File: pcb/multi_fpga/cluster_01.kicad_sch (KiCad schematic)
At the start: 4 parts

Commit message: Fixed library and power issues.
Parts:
- A2: symbol CMOD_S7 -> multi_fpga:CMOD_S7
- C25, C26: symbol C -> multi_fpga:C
- VR1: symbol LDO_1V8 -> Regulator_Linear:MCP1700x-180xxTT
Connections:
- net +5V: no longer VR1.3 (IN)
- net C1_1V8: no longer VR1.2 (OUT)
- net GND: no longer VR1.1 (GND)
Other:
- moved on the sheet: VR1
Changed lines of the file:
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@@
 	)
 	(symbol
-		(lib_id "power:C1_1V8")
+		(lib_id "multi_fpga:C1_1V8")
 		(at 270.51 213.36 0)
 		(unit 1)
@@
 	)
 	(symbol
-		(lib_id "LDO_1V8")
+		(lib_id "Regulator_Linear:MCP1700x-180xxTT")
 		(at 300.99 218.44 0)
 		(unit 1)
@@
 	)
 	(symbol
-		(lib_id "C")
+		(lib_id "multi_fpga:C")
 		(at 326.39 218.44 0)
 		(unit 1)
@@
 	)
 	(symbol
-		(lib_id "power:C1_1V8")
+		(lib_id "multi_fpga:C1_1V8")
 		(at 326.39 214.63 0)
 		(unit 1)
@@
 	)
 	(symbol
-		(lib_id "CMOD_S7")
+		(lib_id "multi_fpga:CMOD_S7")
 		(at 262.89 142.24 0)
 		(unit 1)
@@
 	)
 	(symbol
-		(lib_id "C")
+		(lib_id "multi_fpga:C")
 		(at 255.27 218.44 0)
 		(unit 1)

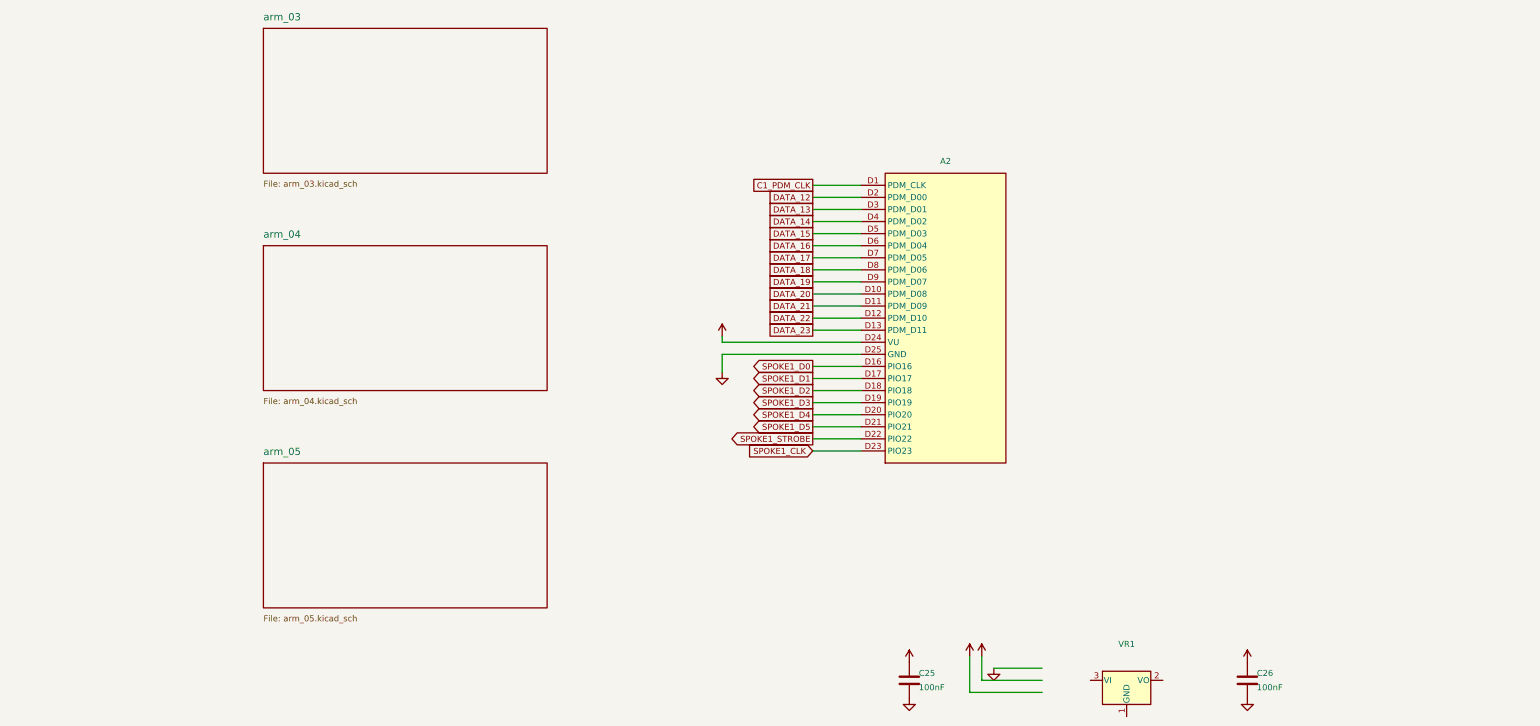
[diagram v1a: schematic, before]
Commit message: Fixed power and C ref des collisions.
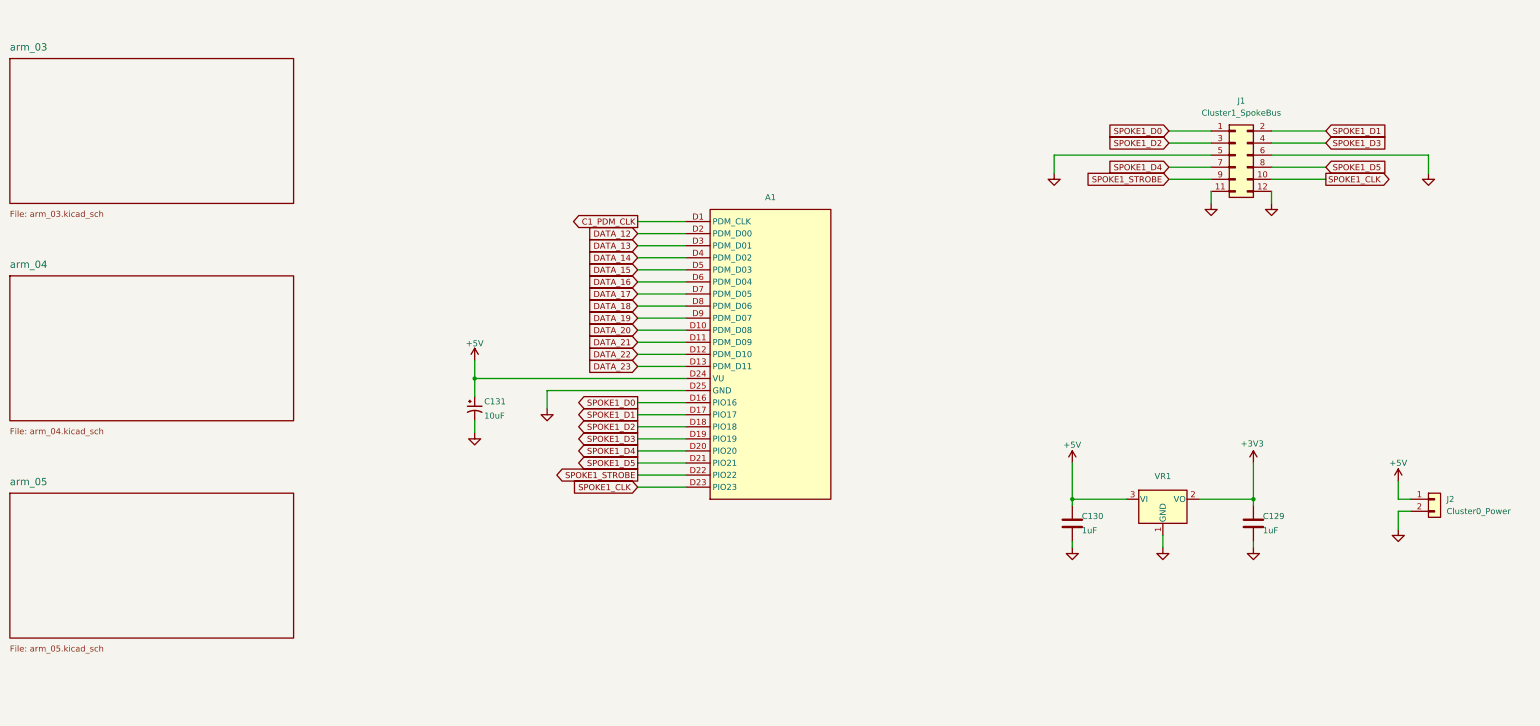
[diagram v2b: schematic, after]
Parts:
- removed C25, C26: 100nF, symbol multi_fpga:C
- added C129, C130: 1uF, Capacitor_SMD:C_0201_0603Metric, symbol multi_fpga:C
- added C131: 10uF, SparkFun-Capacitor:C_0603_1608Metric_Polar, symbol SparkFun-Capacitor:10uF_0603_6.3V_20%_Polar(Tant)
- added J1: Cluster1_SpokeBus, Connector_PinHeader_2.54mm:PinHeader_2x06_P2.54mm_Vertical, symbol Connector_Generic:Conn_02x06_Odd_Even
- added J2: Cluster0_Power, symbol Connector_Generic:Conn_01x02
- renumbered A2 to A1
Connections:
- net +5V: now also VR1.3 (VI), C130.1, C131.1, J2.1 (Pin_1)
- net GND: now also VR1.1 (GND), C129.2, C130.2, C131.2, J1.11 (Pin_11), J1.12 (Pin_12), J1.5 (Pin_5), J1.6 (Pin_6), J2.2 (Pin_2)
- net SPOKE1_CLK: now also J1.10 (Pin_10)
- net SPOKE1_D0: now also J1.1 (Pin_1)
- net SPOKE1_D1: now also J1.2 (Pin_2)
- net SPOKE1_D2: now also J1.3 (Pin_3)
- net SPOKE1_D3: now also J1.4 (Pin_4)
- net SPOKE1_D4: now also J1.7 (Pin_7)
- net SPOKE1_D5: now also J1.8 (Pin_8)
- net SPOKE1_STROBE: now also J1.9 (Pin_9)
- net +3V3: now reaches VR1.2 (VO)
- net +3V3: now also C129.1
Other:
- moved on the sheet: A1

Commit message: Fixed annotations.
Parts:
- renumbered A1 to A2, J1 to J11, J2 to J12, VR1 to VR2
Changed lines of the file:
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@@
+				)
+			)
+			(project "top"
+				(path "/80f109c4-96c5-4385-bfb6-0f7a96b014ab/2fbc7b9e-8fe5-4ac1-bfbb-0f46b8d2fb6e"
+					(reference "C129")
+					(unit 1)
 				)
 			)
@@
 		(in_pos_files yes)
 		(dnp no)
-		(property "Reference" "VR1"
+		(property "Reference" "VR2"
 			(at 308.61 175.514 0)
 			(show_name no)
@@
 			(project "cluster_01"
 				(path "/042ed5be-47f7-4943-a507-c910d450c4ed"
+					(reference "VR2")
+					(unit 1)
+				)
+			)
+			(project "top"
+				(path "/80f109c4-96c5-4385-bfb6-0f7a96b014ab/2fbc7b9e-8fe5-4ac1-bfbb-0f46b8d2fb6e"
 					(reference "VR1")
 					(unit 1)
@@
 				)
 			)
+			(project "top"
+				(path "/80f109c4-96c5-4385-bfb6-0f7a96b014ab/2fbc7b9e-8fe5-4ac1-bfbb-0f46b8d2fb6e"
+					(reference "C130")
+					(unit 1)
+				)
+			)
 		)
 	)
@@
 				)
 			)
+			(project "top"
+				(path "/80f109c4-96c5-4385-bfb6-0f7a96b014ab/2fbc7b9e-8fe5-4ac1-bfbb-0f46b8d2fb6e"
+					(reference "C131")
+					(unit 1)
+				)
+			)
 		)
 	)
@@
 				)
 			)
+			(project "top"
+				(path "/80f109c4-96c5-4385-bfb6-0f7a96b014ab/2fbc7b9e-8fe5-4ac1-bfbb-0f46b8d2fb6e"
+					(reference "#PWR0708")
+					(unit 1)
+				)
+			)
 		)
 	)
@@
 				)
 			)
+			(project "top"
+				(path "/80f109c4-96c5-4385-bfb6-0f7a96b014ab/2fbc7b9e-8fe5-4ac1-bfbb-0f46b8d2fb6e"
+					(reference "#PWR0709")
+					(unit 1)
+				)
+			)
 		)
 	)
@@
 			(project "cluster_01"
 				(path "/042ed5be-47f7-4943-a507-c910d450c4ed"
+					(reference "#PWR0710")
+					(unit 1)
+				)
+			)
+			(project "top"
+				(path "/80f109c4-96c5-4385-bfb6-0f7a96b014ab/2fbc7b9e-8fe5-4ac1-bfbb-0f46b8d2fb6e"
 					(reference "#PWR0710")
 					(unit 1)
@@
 				)
 			)
+			(project "top"
+				(path "/80f109c4-96c5-4385-bfb6-0f7a96b014ab/2fbc7b9e-8fe5-4ac1-bfbb-0f46b8d2fb6e"
+					(reference "#PWR0711")
+					(unit 1)
+				)
+			)
 		)
 	)
@@
 		(dnp no)
 		(fields_autoplaced yes)
-		(property "Reference" "J1"
+		(property "Reference" "J11"
 			(at 325.12 96.52 0)
 			(show_name no)
@@
 			(project "cluster_01"
 				(path "/042ed5be-47f7-4943-a507-c910d450c4ed"
+					(reference "J11")
+					(unit 1)
+				)
+			)
+			(project "top"
+				(path "/80f109c4-96c5-4385-bfb6-0f7a96b014ab/2fbc7b9e-8fe5-4ac1-bfbb-0f46b8d2fb6e"
 					(reference "J1")
 					(unit 1)
@@
 				)
 			)
+			(project "top"
+				(path "/80f109c4-96c5-4385-bfb6-0f7a96b014ab/2fbc7b9e-8fe5-4ac1-bfbb-0f46b8d2fb6e"
+					(reference "#PWR0712")
+					(unit 1)
+				)
+			)
 		)
 	)
@@
 				)
 			)
+			(project "top"
+				(path "/80f109c4-96c5-4385-bfb6-0f7a96b014ab/2fbc7b9e-8fe5-4ac1-bfbb-0f46b8d2fb6e"
+					(reference "#PWR0713")
+					(unit 1)
+				)
+			)
 		)
 	)
@@
 		(dnp no)
 		(fields_autoplaced yes)
-		(property "Reference" "J2"
+		(property "Reference" "J12"
 			(at 368.3 180.3399 0)
 			(show_name no)
@@
 			(project "cluster_01"
 				(path "/042ed5be-47f7-4943-a507-c910d450c4ed"
+					(reference "J12")
+					(unit 1)
+				)
+			)
+			(project "top"
+				(path "/80f109c4-96c5-4385-bfb6-0f7a96b014ab/2fbc7b9e-8fe5-4ac1-bfbb-0f46b8d2fb6e"
 					(reference "J2")
 					(unit 1)
@@
 				)
 			)
+			(project "top"
+				(path "/80f109c4-96c5-4385-bfb6-0f7a96b014ab/2fbc7b9e-8fe5-4ac1-bfbb-0f46b8d2fb6e"
+					(reference "#PWR0714")
+					(unit 1)
+				)
+			)
 		)
 	)
@@
 			(project "cluster_01"
 				(path "/042ed5be-47f7-4943-a507-c910d450c4ed"
+					(reference "#PWR0715")
+					(unit 1)
+				)
+			)
+			(project "top"
+				(path "/80f109c4-96c5-4385-bfb6-0f7a96b014ab/2fbc7b9e-8fe5-4ac1-bfbb-0f46b8d2fb6e"
 					(reference "#PWR0715")
 					(unit 1)
@@
 				)
 			)
+			(project "top"
+				(path "/80f109c4-96c5-4385-bfb6-0f7a96b014ab/2fbc7b9e-8fe5-4ac1-bfbb-0f46b8d2fb6e"
+					(reference "#PWR0716")
+					(unit 1)
+				)
+			)
 		)
 	)
@@
 				)
 			)
+			(project "top"
+				(path "/80f109c4-96c5-4385-bfb6-0f7a96b014ab/2fbc7b9e-8fe5-4ac1-bfbb-0f46b8d2fb6e"
+					(reference "#PWR0717")
+					(unit 1)
+				)
+			)
 		)
 	)
@@
 			(project "cluster_01"
 				(path "/042ed5be-47f7-4943-a507-c910d450c4ed"
+					(reference "#PWR0718")
+					(unit 1)
+				)
+			)
+			(project "top"
+				(path "/80f109c4-96c5-4385-bfb6-0f7a96b014ab/2fbc7b9e-8fe5-4ac1-bfbb-0f46b8d2fb6e"
 					(reference "#PWR0718")
 					(unit 1)
@@
 				)
 			)
+			(project "top"
+				(path "/80f109c4-96c5-4385-bfb6-0f7a96b014ab/2fbc7b9e-8fe5-4ac1-bfbb-0f46b8d2fb6e"
+					(reference "#PWR0719")
+					(unit 1)
+				)
+			)
 		)
 	)
@@
 		(in_pos_files yes)
 		(dnp no)
-		(property "Reference" "A1"
+		(property "Reference" "A2"
 			(at 226.06 116.84 0)
 			(show_name no)
@@
 			(project "cluster_01"
 				(path "/042ed5be-47f7-4943-a507-c910d450c4ed"
-					(reference "A1")
+					(reference "A2")
 					(unit 1)
 				)
@@
 				)
 			)
+			(project "top"
+				(path "/80f109c4-96c5-4385-bfb6-0f7a96b014ab/2fbc7b9e-8fe5-4ac1-bfbb-0f46b8d2fb6e"
+					(reference "#PWR0720")
+					(unit 1)
+				)
+			)
 		)
 	)
@@
 					(reference "#PWR0721")
 					(unit 1)
+				)
+			)
+			(project "top"
+				(path "/80f109c4-96c5-4385-bfb6-0f7a96b014ab/2fbc7b9e-8fe5-4ac1-bfbb-0f46b8d2fb6e"
+					(reference "#PWR0721")
+					(unit 1)

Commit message: Fixed annotation issues.
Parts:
- renumbered J11 to J3, J12 to J4
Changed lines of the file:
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@@
 			(project "top"
 				(path "/80f109c4-96c5-4385-bfb6-0f7a96b014ab/2fbc7b9e-8fe5-4ac1-bfbb-0f46b8d2fb6e"
-					(reference "VR1")
+					(reference "VR2")
 					(unit 1)
 				)
@@
 		(dnp no)
 		(fields_autoplaced yes)
-		(property "Reference" "J11"
+		(property "Reference" "J3"
 			(at 325.12 96.52 0)
 			(show_name no)
@@
 			(project "top"
 				(path "/80f109c4-96c5-4385-bfb6-0f7a96b014ab/2fbc7b9e-8fe5-4ac1-bfbb-0f46b8d2fb6e"
-					(reference "J1")
+					(reference "J3")
 					(unit 1)
 				)
@@
 		(dnp no)
 		(fields_autoplaced yes)
-		(property "Reference" "J12"
+		(property "Reference" "J4"
 			(at 368.3 180.3399 0)
 			(show_name no)
@@
 			(project "top"
 				(path "/80f109c4-96c5-4385-bfb6-0f7a96b014ab/2fbc7b9e-8fe5-4ac1-bfbb-0f46b8d2fb6e"
-					(reference "J2")
+					(reference "J4")
 					(unit 1)
 				)
@@
 		)
 	)
-	(embedded_fonts no)
 )

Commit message: Fixed ref des collisions.
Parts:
- renumbered J3 to J11, J4 to J12
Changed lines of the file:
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@@
 		(dnp no)
 		(fields_autoplaced yes)
-		(property "Reference" "J3"
+		(property "Reference" "J11"
 			(at 325.12 96.52 0)
 			(show_name no)
@@
 		(dnp no)
 		(fields_autoplaced yes)
-		(property "Reference" "J4"
+		(property "Reference" "J12"
 			(at 368.3 180.3399 0)
 			(show_name no)
@@
 		)
 	)
+	(embedded_fonts no)
 )

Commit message: Fixed regulator connection errors and dangling wire.
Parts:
- J12: value Cluster0_Power -> Cluster1_Power
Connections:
- net +3V3 renamed C1_1V8
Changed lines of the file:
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@@
+	)
+	(symbol
+		(lib_id "multi_fpga:C1_1V8")
+		(at 327.66 172.72 0)
+		(unit 1)
+		(body_style 1)
+		(exclude_from_sim no)
+		(in_bom yes)
+		(on_board yes)
+		(in_pos_files yes)
+		(dnp no)
+		(property "Reference" "#PWR0714"
+			(at 327.66 172.72 0)
+			(hide yes)
+			(show_name no)
+			(do_not_autoplace no)
+			(effects
+				(font
+					(size 1.27 1.27)
+				)
+			)
+		)
+		(property "Value" "C1_1V8"
+			(at 327.66 168.91 0)
+			(show_name no)
+			(do_not_autoplace no)
+			(effects
+				(font
+					(size 1.27 1.27)
+				)
+			)
+		)
+		(property "Footprint" ""
+			(at 327.66 172.72 0)
+			(hide yes)
+			(show_name no)
+			(do_not_autoplace no)
+			(effects
+				(font
+					(size 1.27 1.27)
+				)
+			)
+		)
+		(property "Datasheet" ""
+			(at 327.66 172.72 0)
+			(hide yes)
+			(show_name no)
+			(do_not_autoplace no)
+			(effects
+				(font
+					(size 1.27 1.27)
+				)
+			)
+		)
+		(property "Description" ""
+			(at 327.66 172.72 0)
+			(hide yes)
+			(show_name no)
+			(do_not_autoplace no)
+			(effects
+				(font
+					(size 1.27 1.27)
+				)
+			)
+		)
+		(pin "1"
+		)
+		(instances
+			(project "cluster_01"
+				(path "/042ed5be-47f7-4943-a507-c910d450c4ed"
+					(reference "#PWR0714")
+					(unit 1)
+				)
+			)
+			(project "top"
+				(path "/80f109c4-96c5-4385-bfb6-0f7a96b014ab/2fbc7b9e-8fe5-4ac1-bfbb-0f46b8d2fb6e"
+					(reference "#PWR0714")
+					(unit 1)
+				)
+			)
+		)
 	)
 	(symbol
@@
 			)
 		)
-		(property "Value" "Cluster0_Power"
+		(property "Value" "Cluster1_Power"
 			(at 368.3 182.8799 0)
 			(show_name no)
@@
 					(unit 1)
 				)
-			)
-		)
-	)
-	(symbol
-		(lib_id "power:+3V3")
-		(at 327.66 172.72 0)
-		(unit 1)
-		(body_style 1)
-		(exclude_from_sim no)
-		(in_bom yes)
-		(on_board yes)
-		(in_pos_files yes)
-		(dnp no)
-		(property "Reference" "#PWR0714"
-			(at 327.66 172.72 0)
-			(hide yes)
-			(show_name no)
-			(do_not_autoplace no)
-			(effects
-				(font
-					(size 1.27 1.27)
-				)
-			)
-		)
-		(property "Value" "+3V3"
-			(at 327.406 168.656 0)
-			(show_name no)
-			(do_not_autoplace no)
-			(effects
-				(font
-					(size 1.27 1.27)
-				)
-			)
-		)
-		(property "Footprint" ""
-			(at 327.66 172.72 0)
-			(hide yes)
-			(show_name no)
-			(do_not_autoplace no)
-			(effects
-				(font
-					(size 1.27 1.27)
-				)
-			)
-		)
-		(property "Datasheet" ""
-			(at 327.66 172.72 0)
-			(hide yes)
-			(show_name no)
-			(do_not_autoplace no)
-			(effects
-				(font
-					(size 1.27 1.27)
-				)
-			)
-		)
-		(property "Description" ""
-			(at 327.66 172.72 0)
-			(hide yes)
-			(show_name no)
-			(do_not_autoplace no)
-			(effects
-				(font
-					(size 1.27 1.27)
-				)
-			)
-		)
-		(pin "1"
-		)
-		(instances
-			(project "cluster_01"
-				(path "/042ed5be-47f7-4943-a507-c910d450c4ed"
-					(reference "#PWR0714")
-					(unit 1)
-				)
-			)
-			(project "top"
-				(path "/80f109c4-96c5-4385-bfb6-0f7a96b014ab/2fbc7b9e-8fe5-4ac1-bfbb-0f46b8d2fb6e"
-					(reference "#PWR0714")
-					(unit 1)
-				)

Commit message: Added the LDO regulator part numbers.
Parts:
- VR2: value (none) -> MCP1700T-1802E/TT
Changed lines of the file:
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@@
 			)
 		)
-		(property "Value" ""
-			(at 308.61 180.34 0)
+		(property "Value" "MCP1700T-1802E/TT"
+			(at 308.61 172.72 0)
 			(show_name no)
 			(do_not_autoplace no)

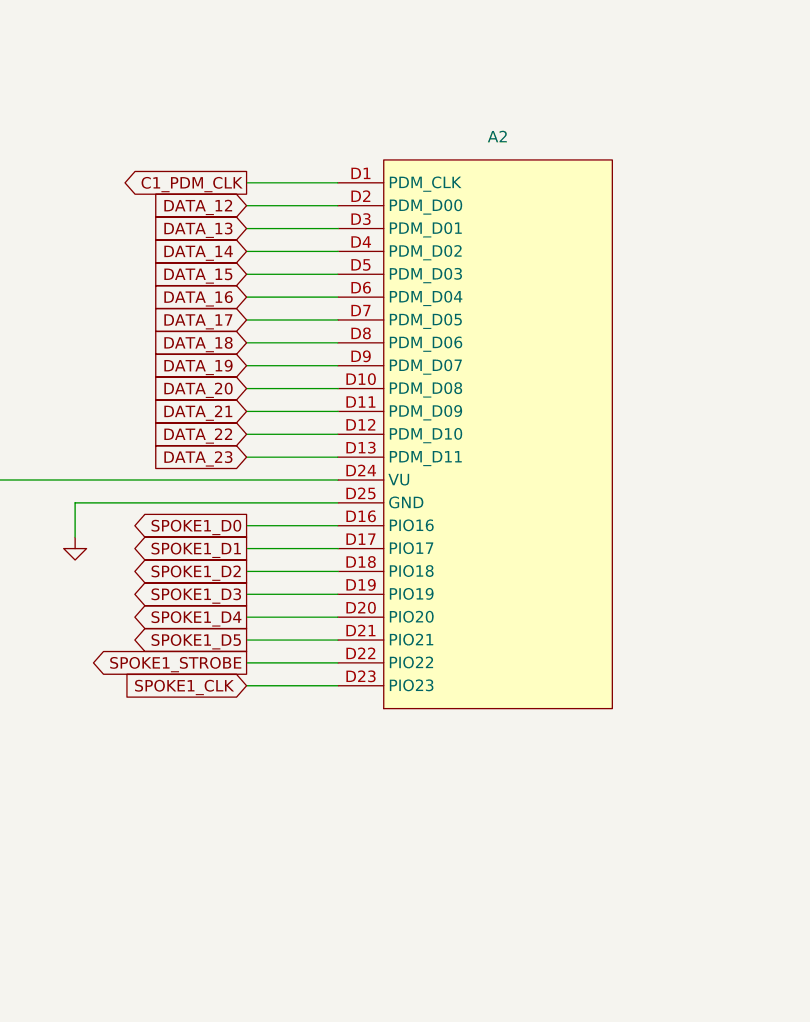
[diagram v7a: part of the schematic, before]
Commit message: Fixed FPGA module symbols.
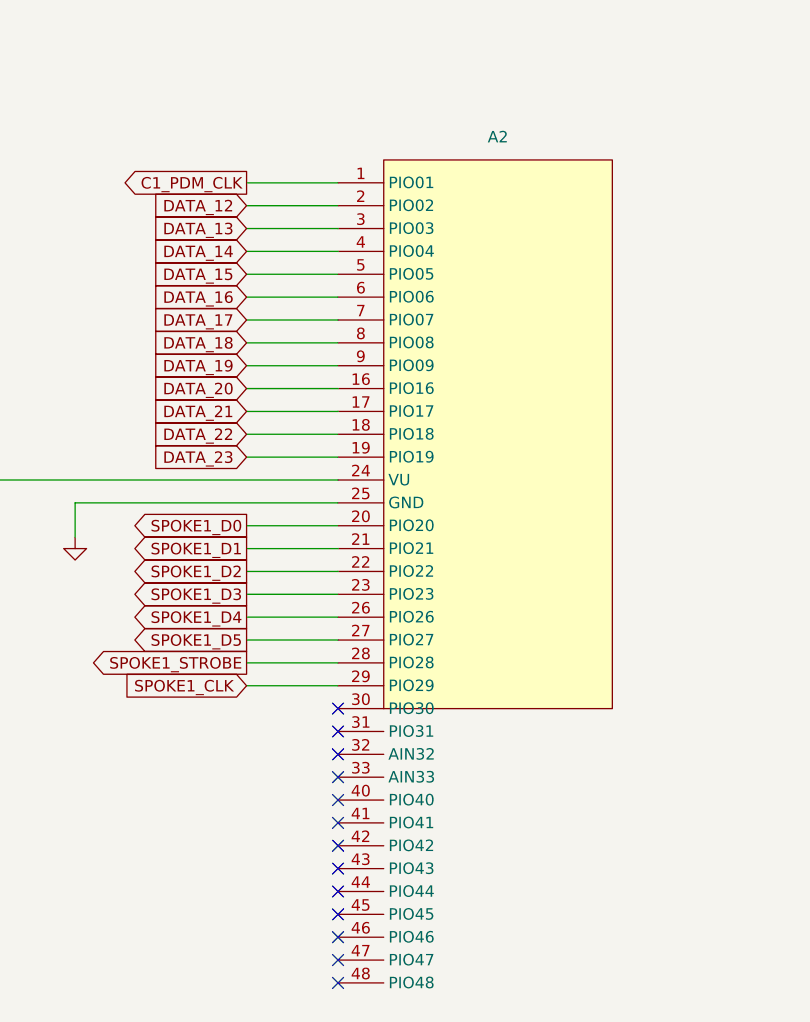
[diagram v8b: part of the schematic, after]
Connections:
- net +5V: now also A2.24 (VU); no longer A2.D24 (VU)
- net C1_PDM_CLK: now also A2.1 (PIO01); no longer A2.D1 (PDM_CLK)
- net DATA_12: now also A2.2 (PIO02); no longer A2.D2 (PDM_D00)
- net DATA_13: now also A2.3 (PIO03); no longer A2.D3 (PDM_D01)
- net DATA_14: now also A2.4 (PIO04); no longer A2.D4 (PDM_D02)
- net DATA_15: now also A2.5 (PIO05); no longer A2.D5 (PDM_D03)
- net DATA_16: now also A2.6 (PIO06); no longer A2.D6 (PDM_D04)
- net DATA_17: now also A2.7 (PIO07); no longer A2.D7 (PDM_D05)
- net DATA_18: now also A2.8 (PIO08); no longer A2.D8 (PDM_D06)
- net DATA_19: now also A2.9 (PIO09); no longer A2.D9 (PDM_D07)
- net DATA_20: now also A2.16 (PIO16); no longer A2.D10 (PDM_D08)
- net DATA_21: now also A2.17 (PIO17); no longer A2.D11 (PDM_D09)
- net DATA_22: now also A2.18 (PIO18); no longer A2.D12 (PDM_D10)
- net DATA_23: now also A2.19 (PIO19); no longer A2.D13 (PDM_D11)
- net GND: now also A2.25 (GND); no longer A2.D25 (GND)
- net SPOKE1_CLK: now also A2.29 (PIO29); no longer A2.D23 (PIO23)
- net SPOKE1_D0: now also A2.20 (PIO20); no longer A2.D16 (PIO16)
- net SPOKE1_D1: now also A2.21 (PIO21); no longer A2.D17 (PIO17)
- net SPOKE1_D2: now also A2.22 (PIO22); no longer A2.D18 (PIO18)
- net SPOKE1_D3: now also A2.23 (PIO23); no longer A2.D19 (PIO19)
- net SPOKE1_D4: now also A2.26 (PIO26); no longer A2.D20 (PIO20)
- net SPOKE1_D5: now also A2.27 (PIO27); no longer A2.D21 (PIO21)
- net SPOKE1_STROBE: now also A2.28 (PIO28); no longer A2.D22 (PIO22)
- no-connect marks 0 -> 13
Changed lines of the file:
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@@
 	)
 	(embedded_fonts no)
+	(no_connect
+		(at 208.28 180.34)
+	)
+	(no_connect
+		(at 208.28 182.88)
+	)
+	(no_connect
+		(at 208.28 185.42)
+	)
+	(no_connect
+		(at 208.28 187.96)
+	)
+	(no_connect
+		(at 208.28 190.5)
+	)
+	(no_connect
+		(at 208.28 193.04)
+	)
+	(no_connect
+		(at 208.28 195.58)
+	)
+	(no_connect
+		(at 208.28 198.12)
+	)
+	(no_connect
+		(at 208.28 200.66)
+	)
+	(no_connect
+		(at 208.28 203.2)
+	)
+	(no_connect
+		(at 208.28 205.74)
+	)
+	(no_connect
+		(at 208.28 208.28)
+	)
+	(no_connect
+		(at 208.28 210.82)
+	)
 )
